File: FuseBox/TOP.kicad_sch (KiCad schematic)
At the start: 54 parts, among them J1 UJ31CHG2SMTTR, U1 TPS61040DBVR, U2 LT3030EFETRPBF

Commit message: some foo
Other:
- added sheet ICE40HX (ICE40HX.kicad_sch)
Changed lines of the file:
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@@
 	)
 	(sheet
-		(at 176.53 152.4)
-		(size 34.29 6.35)
+		(at 306.07 12.7)
+		(size 27.94 6.35)
+		(exclude_from_sim no)
+		(in_bom yes)
+		(on_board yes)
+		(dnp no)
+		(fields_autoplaced yes)
+		(stroke
+			(width 0.1524)
+			(type solid)
+		)
+		(fill
+			(color 0 0 0 0.0000)
+		)
+		(property "Sheetname" "ICE40HX"
+			(at 306.07 11.9884 0)
+			(effects
+				(font
+					(size 1.27 1.27)
+				)
+				(justify left bottom)
+			)
+		)
+		(property "Sheetfile" "ICE40HX.kicad_sch"
+			(at 306.07 19.6346 0)
+			(effects
+				(font
+					(size 1.27 1.27)
+				)
+				(justify left top)
+			)
+		)
+		(instances
+			(project "FuseBox"
+				(path "/7cec0856-4a31-46c4-b6e3-cba19fcff38c"
+					(page "3")
+				)
+			)
+		)
+	)
+	(sheet
+		(at 306.07 0)
+		(size 27.94 6.35)
 		(exclude_from_sim no)
 		(in_bom yes)
@@
 		)
 		(property "Sheetname" "STM32F4"
-			(at 176.53 151.6884 0)
+			(at 306.07 -0.7116 0)
 			(effects
 				(font
@@
 		)
 		(property "Sheetfile" "STM32F4.kicad_sch"
-			(at 176.53 159.3346 0)
+			(at 306.07 6.9346 0)
 			(effects
 				(font

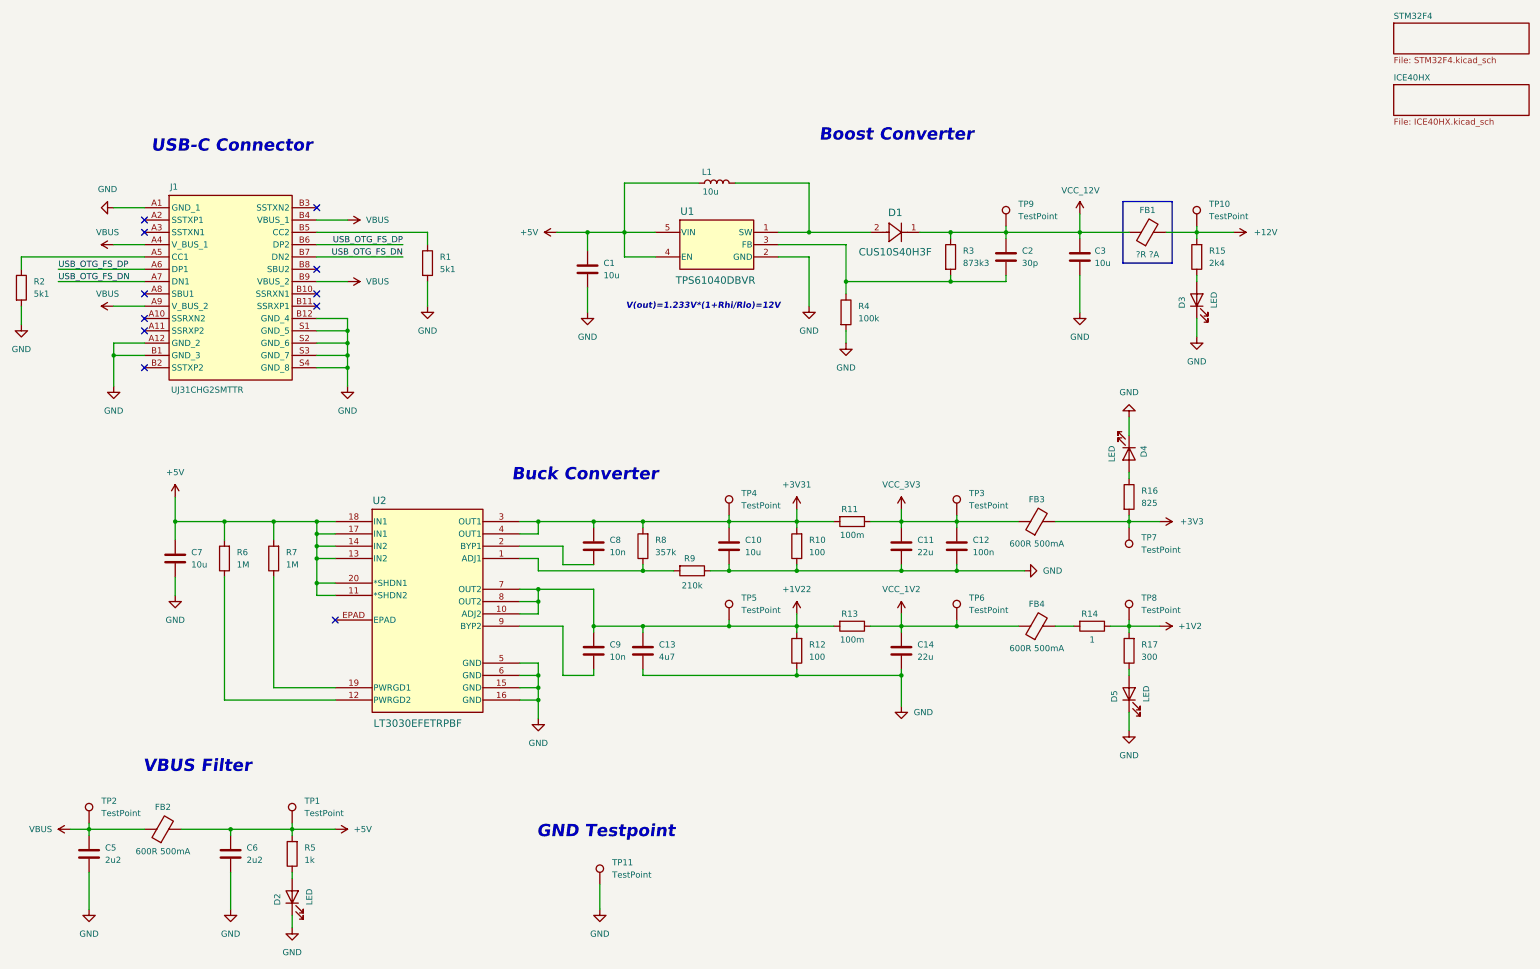
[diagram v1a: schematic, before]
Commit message: added ICE40HX
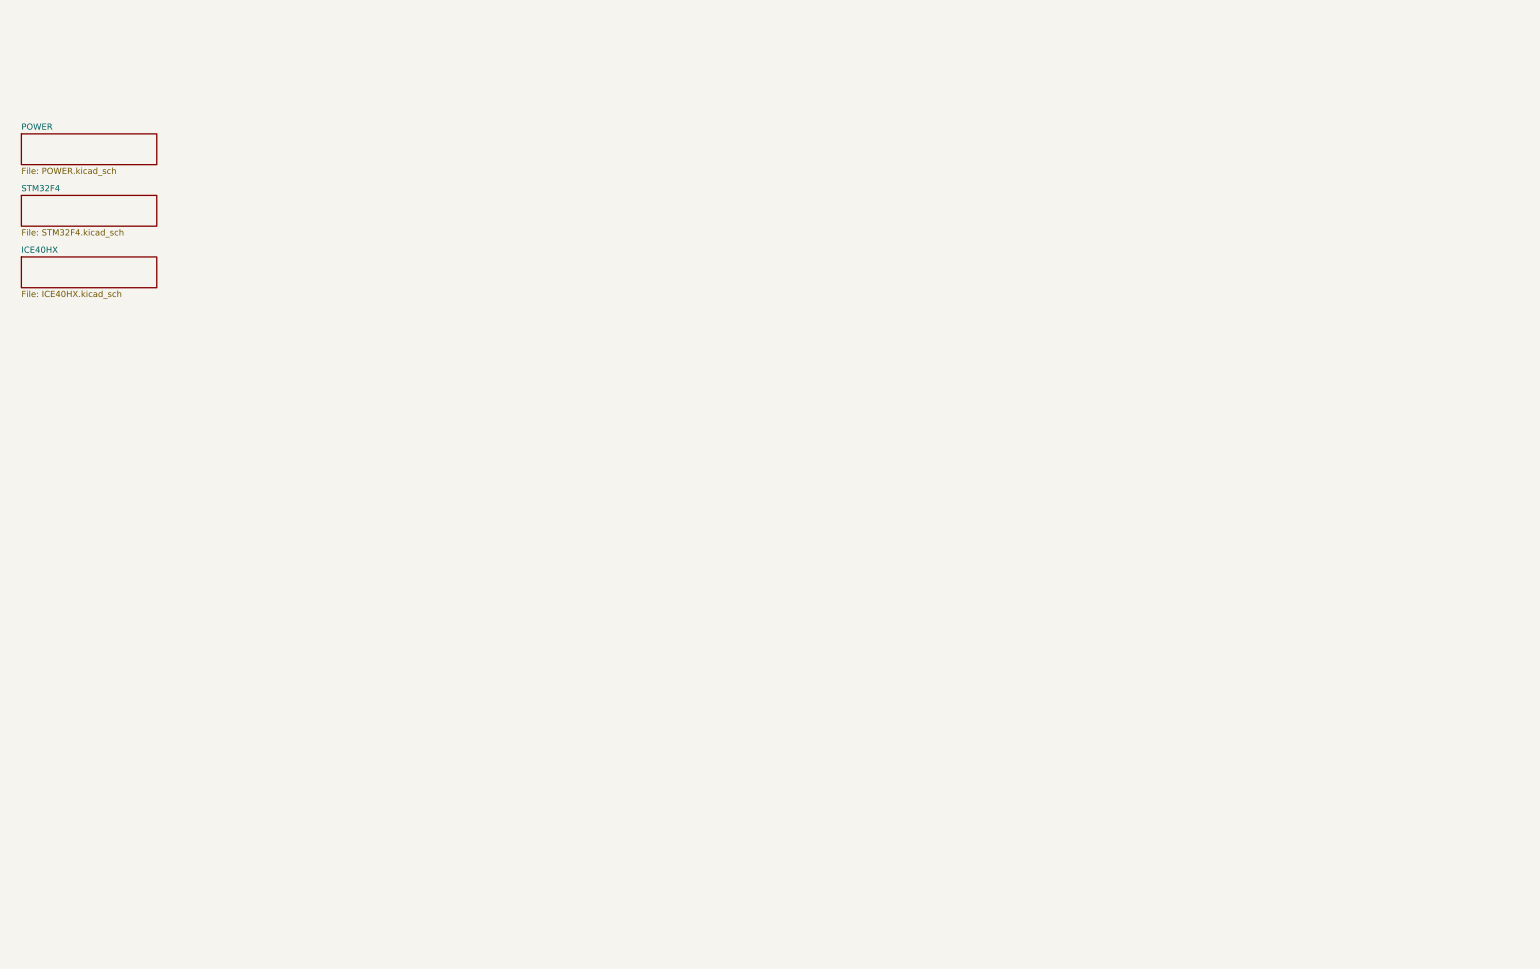
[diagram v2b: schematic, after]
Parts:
- removed C1, C10, C3, C7: 10u, symbol Device:C
- removed C11, C14: 22u, symbol Device:C
- removed C12: 100n, symbol Device:C
- removed C13: 4u7, symbol Device:C
- removed C2: 30p, symbol Device:C
- removed C5, C6: 2u2, symbol Device:C
- removed C8, C9: 10n, symbol Device:C
- removed D1: CUS10S40H3F, Custom:CUS10S40H3F, symbol Custom:CUS10S40H3F
- removed D2, D3, D4, D5: LED, symbol Device:LED
- removed FB1: ?R ?A, symbol Device:FerriteBead
- removed FB2, FB3, FB4: 600R 500mA, symbol Device:FerriteBead
- removed J1: UJ31CHG2SMTTR, Custom:UJ31CHG2SMTTR, symbol Custom:UJ31CHG2SMTTR
- removed L1: 10u, symbol Device:L
- removed R1, R2: 5k1, symbol Device:R
- removed R10, R12: 100, symbol Device:R
- removed R11, R13: 100m, symbol Device:R
- removed R14: 1, symbol Device:R
- removed R15: 2k4, symbol Device:R
- removed R16: 825, symbol Device:R
- removed R17: 300, symbol Device:R
- removed R3: 873k3, symbol Device:R
- removed R4: 100k, symbol Device:R
- removed R5: 1k, symbol Device:R
- removed R6, R7: 1M, symbol Device:R
- removed R8: 357k, symbol Device:R
- removed R9: 210k, symbol Device:R
- removed TP1, TP10, TP11, TP2, TP3, TP4, TP5, TP6, TP7, TP8, TP9: TestPoint, symbol Connector:TestPoint
- removed U1: TPS61040DBVR, Custom:TPS61040DBVR, symbol Custom:TPS61040DBVR
- removed U2: LT3030EFETRPBF, Custom:LT8302ES8ETRPBF, symbol Custom:LT3030EFETRPBF
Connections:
- no-connect marks 11 -> 0
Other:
- added sheet POWER (POWER.kicad_sch)
- note removed: "Boost Converter"
- note removed: "Buck Converter"
- note removed: "GND Testpoint"
- note removed: "USB-C Connector"
- note removed: "V(out)=1.233V*(1+Rhi/Rlo)=12V"
- note removed: "VBUS Filter"

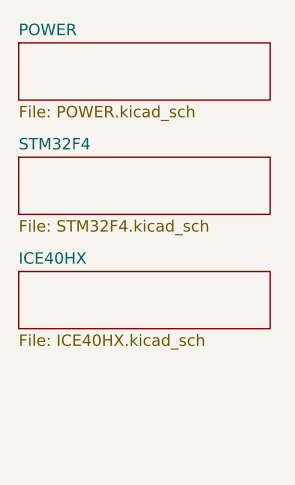
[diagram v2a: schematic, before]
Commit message: added temp USB controllers
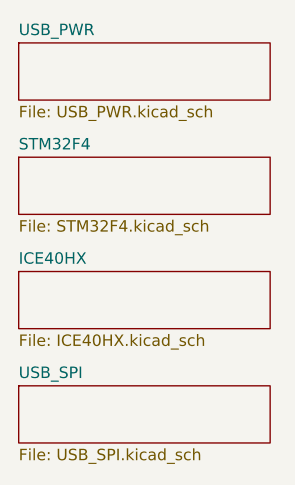
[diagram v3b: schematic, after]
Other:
- sheet POWER renamed USB_PWR
- added sheet USB_SPI (USB_SPI.kicad_sch)
- sheet USB_PWR: file POWER.kicad_sch -> USB_PWR.kicad_sch
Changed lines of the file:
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@@
 	(paper "A4")
+	(sheet
+		(at 22.86 60.96)
+		(size 27.94 6.35)
+		(exclude_from_sim no)
+		(in_bom yes)
+		(on_board yes)
+		(dnp no)
+		(fields_autoplaced yes)
+		(stroke
+			(width 0.1524)
+			(type solid)
+		)
+		(fill
+			(color 0 0 0 0.0000)
+		)
+		(property "Sheetname" "USB_SPI"
+			(at 22.86 60.2484 0)
+			(effects
+				(font
+					(size 1.27 1.27)
+				)
+				(justify left bottom)
+			)
+		)
+		(property "Sheetfile" "USB_SPI.kicad_sch"
+			(at 22.86 67.8946 0)
+			(effects
+				(font
+					(size 1.27 1.27)
+				)
+				(justify left top)
+			)
+		)
+		(instances
+			(project "TOP"
+				(path "/7cec0856-4a31-46c4-b6e3-cba19fcff38c"
+					(page "5")
+				)
+			)
+		)
+	)
 	(sheet
 		(at 22.86 22.86)
@@
 			(color 0 0 0 0.0000)
 		)
-		(property "Sheetname" "POWER"
+		(property "Sheetname" "USB_PWR"
 			(at 22.86 22.1484 0)
 			(effects
@@
 			)
 		)
-		(property "Sheetfile" "POWER.kicad_sch"
+		(property "Sheetfile" "USB_PWR.kicad_sch"
 			(at 22.86 29.7946 0)
 			(effects
